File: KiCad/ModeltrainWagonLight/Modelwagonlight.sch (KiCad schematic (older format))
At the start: 13 parts, among them J1 Conn_01x02, J2 Conn_01x02, U1 NCP1117-ADJ_SOT223

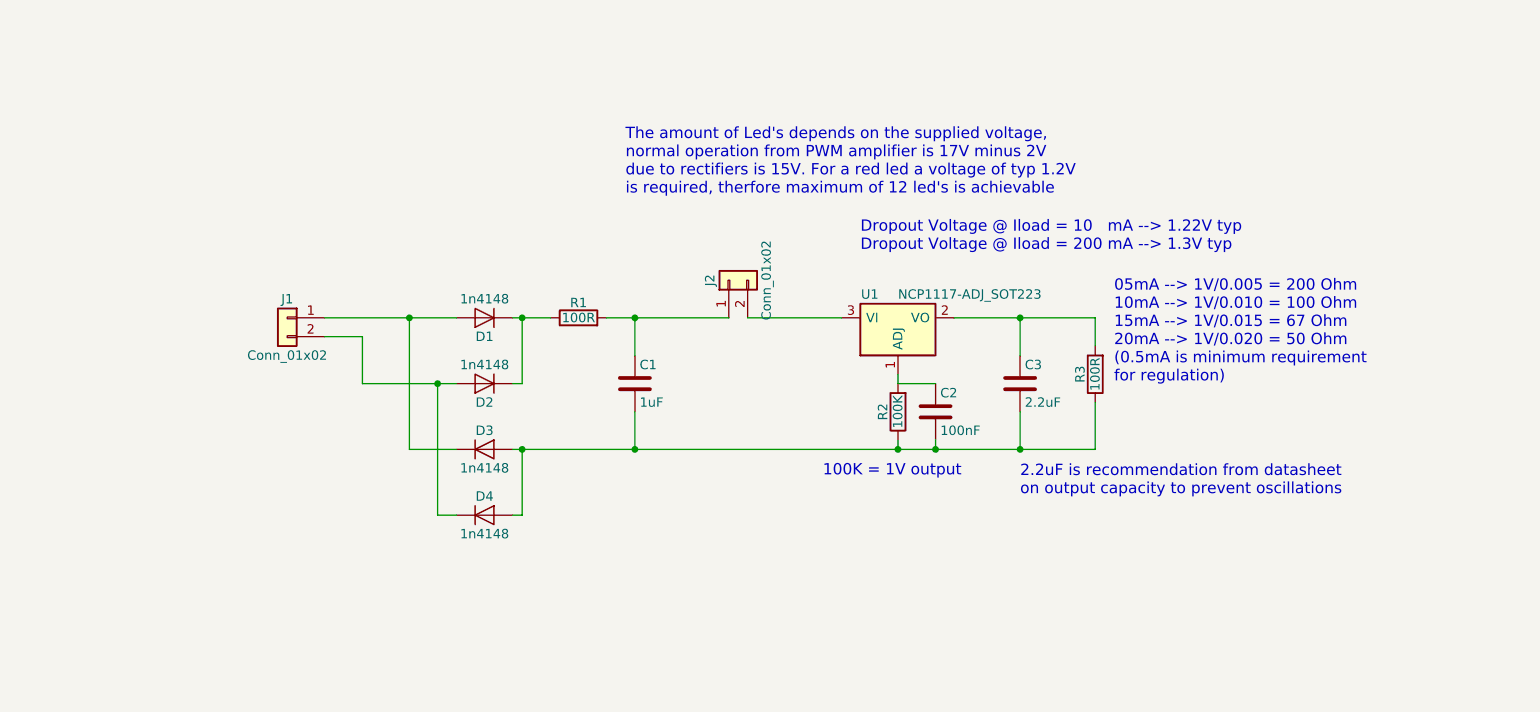
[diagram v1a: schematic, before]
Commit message: Updated ModeltrainWagonLight/Modelwagonlight
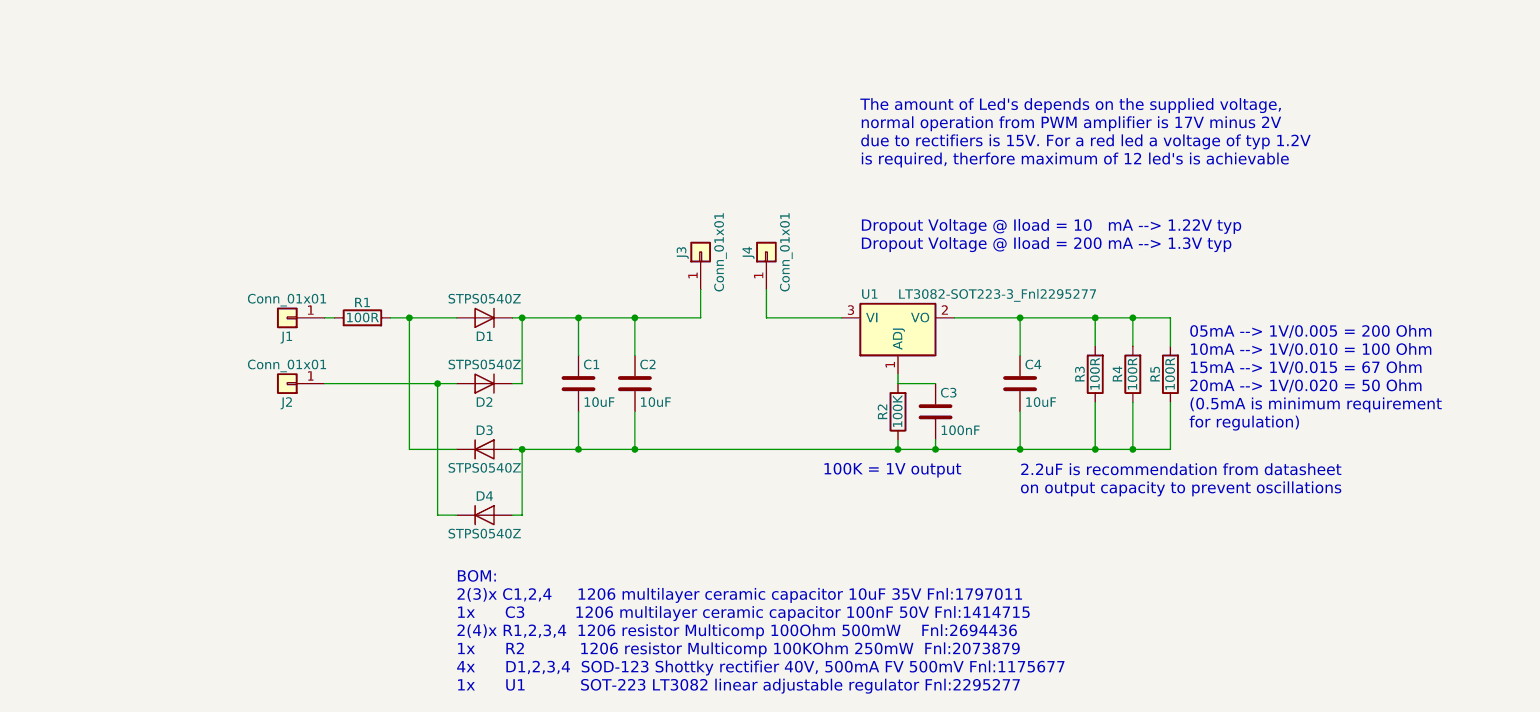
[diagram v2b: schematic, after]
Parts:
- removed J1, J2: Conn_01x02, Pin_Headers:Pin_Header_Angled_1x02_Pitch1.00mm, symbol Conn_01x02
- added C4: 10uF, Capacitors_SMD:C_1206_HandSoldering, symbol C
- added J1, J2, J3, J4: Conn_01x01, Pin_Headers:Pin_Header_Straight_1x01_Pitch1.00mm, symbol Conn_01x01
- added R4, R5: 100R, Resistors_SMD:R_1206_HandSoldering, symbol R
- C1: value 1uF -> 10uF; footprint Capacitors_SMD:C_0805_HandSoldering -> Capacitors_SMD:C_1206_HandSoldering
- C2: value 100nF -> 10uF; footprint Capacitors_SMD:C_0805_HandSoldering -> Capacitors_SMD:C_1206_HandSoldering
- C3: value 2.2uF -> 100nF; footprint Capacitors_SMD:C_0805_HandSoldering -> Capacitors_SMD:C_1206_HandSoldering
- D1, D2, D3, D4: value 1n4148 -> STPS0540Z; footprint Diodes_SMD:D_SOD-323 -> Diodes_SMD:D_SOD-123
- R1, R2, R3: footprint Resistors_SMD:R_0805_HandSoldering -> Resistors_SMD:R_1206_HandSoldering
- U1: value NCP1117-ADJ_SOT223 -> LT3082-SOT223-3_Fnl2295277
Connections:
- net at D1.1 (K), D2.1 (K): now also C1.1, C2.1, J3.1 (Pin_1); no longer R1.1
- net at D2.2 (A), D4.1 (K): now also J2.1 (Pin_1)
- net at D1.2 (A), D3.1 (K): now also R1.2
- net at C1.2, C2.2, C3.2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: now also C4.2, R4.1, R5.1
- net at R2.2, U1.1 (ADJ): now also C3.1; no longer C2.1
- net at R3.2, U1.2 (VO): now also C4.1, R4.2, R5.2; no longer C3.1
- net at U1.3 (VI): now also J4.1 (Pin_1)
- new net: J1.1 (Pin_1), R1.1
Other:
- note added: "BOM:\n2(3)x C1,2,4 1206 multilayer ceramic capacitor 10uF 35V Fnl:1797011\n1x C3 1206 multilayer ceramic capacitor 100nF 50V Fnl:1414715\n2(4)x R1,2,3,4 1206 resistor Multicomp 100Ohm 500mW Fnl:2694436\n1x R2 1206 resistor Multicomp 100KOhm 250mW Fnl:2073879\n4x D1,2,3,4 SOD-123 Shottky rectifier 40V, 500mA FV 500mV Fnl:1175677\n1x U1 SOT-223 LT3082 linear adjustable regulator Fnl:2295277"
- moved on the sheet: R1
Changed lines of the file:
@@
 P 5100 4300
 F 0 "D2" H 5100 4400 50  0000 C CNN
-F 1 "1n4148" H 5100 4200 50  0000 C CNN
-F 2 "Diodes_SMD:D_SOD-323" H 5100 4300 50  0001 C CNN
+F 1 "STPS0540Z" H 5100 4200 50  0000 C CNN
+F 2 "Diodes_SMD:D_SOD-123" H 5100 4300 50  0001 C CNN
 F 3 "" H 5100 4300 50  0001 C CNN
 	1    5100 4300
@@
 P 5100 3950
 F 0 "D1" H 5100 4050 50  0000 C CNN
-F 1 "1n4148" H 5100 3850 50  0000 C CNN
-F 2 "Diodes_SMD:D_SOD-323" H 5100 3950 50  0001 C CNN
+F 1 "STPS0540Z" H 5100 3850 50  0000 C CNN
+F 2 "Diodes_SMD:D_SOD-123" H 5100 3950 50  0001 C CNN
 F 3 "" H 5100 3950 50  0001 C CNN
 	1    5100 3950
@@
 P 5100 5000
 F 0 "D4" H 5100 5100 50  0000 C CNN
-F 1 "1n4148" H 5100 4900 50  0000 C CNN
-F 2 "Diodes_SMD:D_SOD-323" H 5100 5000 50  0001 C CNN
+F 1 "STPS0540Z" H 5100 4900 50  0000 C CNN
+F 2 "Diodes_SMD:D_SOD-123" H 5100 5000 50  0001 C CNN
 F 3 "" H 5100 5000 50  0001 C CNN
 	1    5100 5000
@@
 P 5100 4650
 F 0 "D3" H 5100 4750 50  0000 C CNN
-F 1 "1n4148" H 5100 4550 50  0000 C CNN
-F 2 "Diodes_SMD:D_SOD-323" H 5100 4650 50  0001 C CNN
+F 1 "STPS0540Z" H 5100 4550 50  0000 C CNN
+F 2 "Diodes_SMD:D_SOD-123" H 5100 4650 50  0001 C CNN
 F 3 "" H 5100 4650 50  0001 C CNN
 	1    5100 4650
@@
 L R R1
 U 1 1 5A952272
-P 5600 3950
-F 0 "R1" V 5680 3950 50  0000 C CNN
-F 1 "100R" V 5600 3950 50  0000 C CNN
-F 2 "Resistors_SMD:R_0805_HandSoldering" V 5530 3950 50  0001 C CNN
-F 3 "" H 5600 3950 50  0001 C CNN
-	1    5600 3950
+P 4450 3950
+F 0 "R1" V 4530 3950 50  0000 C CNN
+F 1 "100R" V 4450 3950 50  0000 C CNN
+F 2 "Resistors_SMD:R_1206_HandSoldering" V 4380 3950 50  0001 C CNN
+F 3 "" H 4450 3950 50  0001 C CNN
+	1    4450 3950
 	0    -1   -1   0
 $EndComp
@@
 F 0 "R2" V 7380 4450 50  0000 C CNN
 F 1 "100K" V 7300 4450 50  0000 C CNN
-F 2 "Resistors_SMD:R_0805_HandSoldering" V 7230 4450 50  0001 C CNN
+F 2 "Resistors_SMD:R_1206_HandSoldering" V 7230 4450 50  0001 C CNN
 F 3 "" H 7300 4450 50  0001 C CNN
 	1    7300 4450
@@
 $EndComp
 Wire Wire Line
-	5250 3950 5450 3950
-Wire Wire Line
-	5250 4650 8350 4650
+	5250 3950 6250 3950
+Wire Wire Line
+	5250 4650 8750 4650
 Wire Wire Line
 	5300 5000 5250 5000
@@
 	4850 5000 4950 5000
 Connection ~ 4850 4300
-$Comp
-L C C1
-U 1 1 5A953B73
-P 5900 4300
-F 0 "C1" H 5925 4400 50  0000 L CNN
-F 1 "1uF" H 5925 4200 50  0000 L CNN
-F 2 "Capacitors_SMD:C_0805_HandSoldering" H 5938 4150 50  0001 C CNN
-F 3 "" H 5900 4300 50  0001 C CNN
-	1    5900 4300
-	1    0    0    -1
-$EndComp
-Wire Wire Line
-	4250 3950 4950 3950
-Wire Wire Line
-	4450 4300 4950 4300
+Wire Wire Line
+	4250 4300 4950 4300
 $Comp
 L NCP1117-ADJ_SOT223 U1
@@
 P 7300 3950
 F 0 "U1" H 7150 4075 50  0000 C CNN
-F 1 "NCP1117-ADJ_SOT223" H 7300 4075 50  0000 L CNN
+F 1 "LT3082-SOT223-3_Fnl2295277" H 7300 4075 50  0000 L CNN
 F 2 "TO_SOT_Packages_SMD:SOT-223-3_TabPin2" H 7300 4150 50  0001 C CNN
 F 3 "" H 7400 3700 50  0001 C CNN
@@
 F 0 "R3" V 8430 4250 50  0000 C CNN
 F 1 "100R" V 8350 4250 50  0000 C CNN
-F 2 "Resistors_SMD:R_0805_HandSoldering" V 8280 4250 50  0001 C CNN
+F 2 "Resistors_SMD:R_1206_HandSoldering" V 8280 4250 50  0001 C CNN
 F 3 "" H 8350 4250 50  0001 C CNN
 	1    8350 4250
@@
 $EndComp
 Wire Wire Line
-	7600 3950 8350 3950
+	7600 3950 8750 3950
 Wire Wire Line
 	8350 3950 8350 4100
 Text Notes 6900 4800 0    60   ~ 0
 100K = 1V output
-Text Notes 8450 4300 0    60   ~ 0
+Text Notes 8850 4550 0    60   ~ 0
 05mA --> 1V/0.005 = 200 Ohm\n10mA --> 1V/0.010 = 100 Ohm\n15mA --> 1V/0.015 = 67 Ohm\n20mA --> 1V/0.020 = 50 Ohm\n(0.5mA is minimum requirement \nfor regulation)
 Text Notes 7100 3600 0    60   ~ 0
 Dropout Voltage @ Iload = 10   mA --> 1.22V typ\nDropout Voltage @ Iload = 200 mA --> 1.3V typ
-$Comp
-L C C2
-U 1 1 5AB3CFB6
-P 7500 4450
-F 0 "C2" H 7525 4550 50  0000 L CNN
-F 1 "100nF" H 7525 4350 50  0000 L CNN
-F 2 "Capacitors_SMD:C_0805_HandSoldering" H 7538 4300 50  0001 C CNN
-F 3 "" H 7500 4450 50  0001 C CNN
-	1    7500 4450
-	1    0    0    -1
-$EndComp
 Connection ~ 7500 4650
 Wire Wire Line
@@
 	5900 4450 5900 4650
 Connection ~ 5900 4650
-$Comp
-L C C3
-U 1 1 5AB3DBE0
-P 7950 4300
-F 0 "C3" H 7975 4400 50  0000 L CNN
-F 1 "2.2uF" H 7975 4200 50  0000 L CNN
-F 2 "Capacitors_SMD:C_0805_HandSoldering" H 7988 4150 50  0001 C CNN
-F 3 "" H 7950 4300 50  0001 C CNN
-	1    7950 4300
-	1    0    0    -1
-$EndComp
 Wire Wire Line
 	7950 4150 7950 3950
@@
 Text Notes 7950 4900 0    60   ~ 0
 2.2uF is recommendation from datasheet \non output capacity to prevent oscillations\n
-Text Notes 5850 3300 0    60   ~ 0
+Text Notes 7100 3150 0    60   ~ 0
 The amount of Led's depends on the supplied voltage,\nnormal operation from PWM amplifier is 17V minus 2V \ndue to rectifiers is 15V. For a red led a voltage of typ 1.2V\nis required, therfore maximum of 12 led's is achievable
 Wire Wire Line
 	7500 4600 7500 4650
-$Comp
-L Conn_01x02 J1
-U 1 1 5AB3E9A3
+Wire Wire Line
+	6600 3950 7000 3950
+Wire Wire Line
+	4250 3950 4300 3950
+Wire Wire Line
+	4600 3950 4950 3950
+$Comp
+L R R4
+U 1 1 5ABB5CE8
+P 8550 4250
+F 0 "R4" V 8630 4250 50  0000 C CNN
+F 1 "100R" V 8550 4250 50  0000 C CNN
+F 2 "Resistors_SMD:R_1206_HandSoldering" V 8480 4250 50  0001 C CNN
+F 3 "" H 8550 4250 50  0001 C CNN
+	1    8550 4250
+	-1   0    0    1
+$EndComp
+$Comp
+L R R5
+U 1 1 5ABB5D36
+P 8750 4250
+F 0 "R5" V 8830 4250 50  0000 C CNN
+F 1 "100R" V 8750 4250 50  0000 C CNN
+F 2 "Resistors_SMD:R_1206_HandSoldering" V 8680 4250 50  0001 C CNN
+F 3 "" H 8750 4250 50  0001 C CNN
+	1    8750 4250
+	-1   0    0    1
+$EndComp
+Wire Wire Line
+	8550 3950 8550 4100
+Connection ~ 8350 3950
+Wire Wire Line
+	8750 3950 8750 4100
+Connection ~ 8550 3950
+Wire Wire Line
+	8550 4650 8550 4400
+Connection ~ 8350 4650
+Wire Wire Line
+	8750 4650 8750 4400
+Connection ~ 8550 4650
+Wire Wire Line
+	5600 4150 5600 3950
+Connection ~ 5600 3950
+Wire Wire Line
+	5600 4450 5600 4650
+Connection ~ 5600 4650
+Text Notes 4950 5950 0    60   ~ 0
+BOM:\n2(3)x C1,2,4     1206 multilayer ceramic capacitor 10uF 35V Fnl:1797011\n1x      C3          1206 multilayer ceramic capacitor 100nF 50V Fnl:1414715\n2(4)x R1,2,3,4  1206 resistor Multicomp 100Ohm 500mW    Fnl:2694436\n1x      R2           1206 resistor Multicomp 100KOhm 250mW  Fnl:2073879\n4x      D1,2,3,4  SOD-123 Shottky rectifier 40V, 500mA FV 500mV Fnl:1175677\n1x      U1           SOT-223 LT3082 linear adjustable regulator Fnl:2295277
+$Comp
+L C C1
+U 1 1 5ABB8BA8
+P 5600 4300
+F 0 "C1" H 5625 4400 50  0000 L CNN
+F 1 "10uF" H 5625 4200 50  0000 L CNN
+F 2 "Capacitors_SMD:C_1206_HandSoldering" H 5638 4150 50  0001 C CNN
+F 3 "" H 5600 4300 50  0001 C CNN
+	1    5600 4300
+	1    0    0    -1
+$EndComp
+$Comp
+L C C2
+U 1 1 5ABB8CAB
+P 5900 4300
+F 0 "C2" H 5925 4400 50  0000 L CNN
+F 1 "10uF" H 5925 4200 50  0000 L CNN
+F 2 "Capacitors_SMD:C_1206_HandSoldering" H 5938 4150 50  0001 C CNN
+F 3 "" H 5900 4300 50  0001 C CNN
+	1    5900 4300
+	1    0    0    -1
+$EndComp
+$Comp
+L C C3
+U 1 1 5ABB8D4D
+P 7500 4450
+F 0 "C3" H 7525 4550 50  0000 L CNN
+F 1 "100nF" H 7525 4350 50  0000 L CNN
+F 2 "Capacitors_SMD:C_1206_HandSoldering" H 7538 4300 50  0001 C CNN
+F 3 "" H 7500 4450 50  0001 C CNN
+	1    7500 4450
+	1    0    0    -1
+$EndComp
+$Comp
+L C C4
+U 1 1 5ABB8DA0
+P 7950 4300
+F 0 "C4" H 7975 4400 50  0000 L CNN
+F 1 "10uF" H 7975 4200 50  0000 L CNN
+F 2 "Capacitors_SMD:C_1206_HandSoldering" H 7988 4150 50  0001 C CNN
+F 3 "" H 7950 4300 50  0001 C CNN
+	1    7950 4300
+	1    0    0    -1
+$EndComp
+$Comp
+L Conn_01x01 J1
+U 1 1 5ABBBE6F
 P 4050 3950
 F 0 "J1" H 4050 4050 50  0000 C CNN
-F 1 "Conn_01x02" H 4050 3750 50  0000 C CNN
-F 2 "Pin_Headers:Pin_Header_Angled_1x02_Pitch1.00mm" H 4050 3950 50  0001 C CNN
+F 1 "Conn_01x01" H 4050 3850 50  0000 C CNN
+F 2 "Pin_Headers:Pin_Header_Straight_1x01_Pitch1.00mm" H 4050 3950 50  0001 C CNN
 F 3 "" H 4050 3950 50  0001 C CNN
 	1    4050 3950
-	-1   0    0    -1
-$EndComp
-$Comp
-L Conn_01x02 J2
-U 1 1 5AB3EB44
-P 6400 3750
-F 0 "J2" H 6400 3850 50  0000 C CNN
-F 1 "Conn_01x02" H 6400 3550 50  0000 C CNN
-F 2 "Pin_Headers:Pin_Header_Angled_1x02_Pitch1.00mm" H 6400 3750 50  0001 C CNN
-F 3 "" H 6400 3750 50  0001 C CNN
-	1    6400 3750
+	-1   0    0    1
+$EndComp
+$Comp
+L Conn_01x01 J2
+U 1 1 5ABBBEC0
+P 4050 4300
+F 0 "J2" H 4050 4400 50  0000 C CNN
+F 1 "Conn_01x01" H 4050 4200 50  0000 C CNN
+F 2 "Pin_Headers:Pin_Header_Straight_1x01_Pitch1.00mm" H 4050 4300 50  0001 C CNN
+F 3 "" H 4050 4300 50  0001 C CNN
+	1    4050 4300
+	-1   0    0    1
+$EndComp
+$Comp
+L Conn_01x01 J3
+U 1 1 5ABBC0DE
+P 6250 3600
+F 0 "J3" H 6250 3700 50  0000 C CNN
+F 1 "Conn_01x01" H 6250 3500 50  0000 C CNN
+F 2 "Pin_Headers:Pin_Header_Straight_1x01_Pitch1.00mm" H 6250 3600 50  0001 C CNN
+F 3 "" H 6250 3600 50  0001 C CNN
+	1    6250 3600
 	0    -1   -1   0
 $EndComp
-Wire Wire Line
-	5750 3950 6400 3950
-Wire Wire Line
-	6500 3950 7000 3950
-Wire Wire Line
-	4250 4050 4450 4050
-Wire Wire Line
-	4450 4050 4450 4300
+$Comp
+L Conn_01x01 J4
+U 1 1 5ABBC139
+P 6600 3600
+F 0 "J4" H 6600 3700 50  0000 C CNN
+F 1 "Conn_01x01" H 6600 3500 50  0000 C CNN
+F 2 "Pin_Headers:Pin_Header_Straight_1x01_Pitch1.00mm" H 6600 3600 50  0001 C CNN
+F 3 "" H 6600 3600 50  0001 C CNN
+	1    6600 3600
+	0    -1   -1   0
+$EndComp
+Wire Wire Line
+	6250 3950 6250 3800
+Wire Wire Line
+	6600 3800 6600 3950
 $EndSCHEMATC
